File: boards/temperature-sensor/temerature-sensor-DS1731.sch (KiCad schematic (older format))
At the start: 2 parts

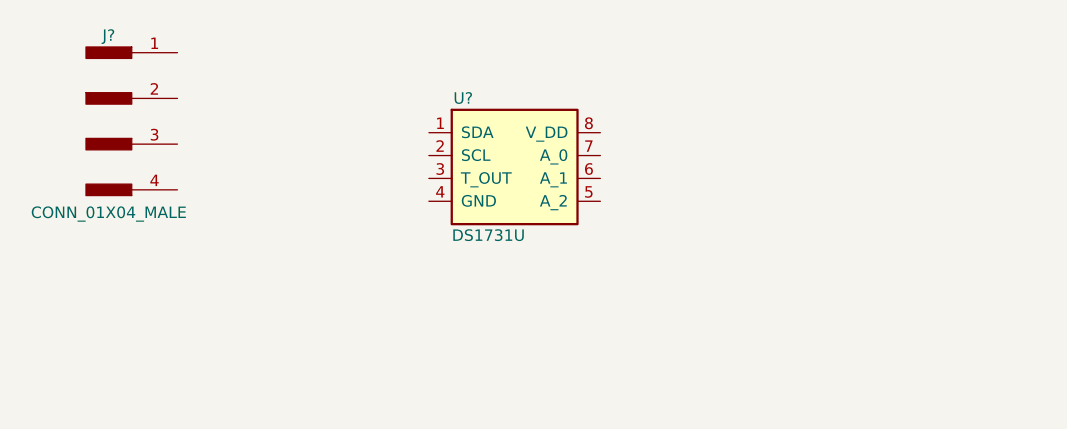
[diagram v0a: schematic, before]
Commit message: schematic completed
build the nessecary schematics, including a resistor Network to pull
address selector pins up or down using 0 and 10k resistors
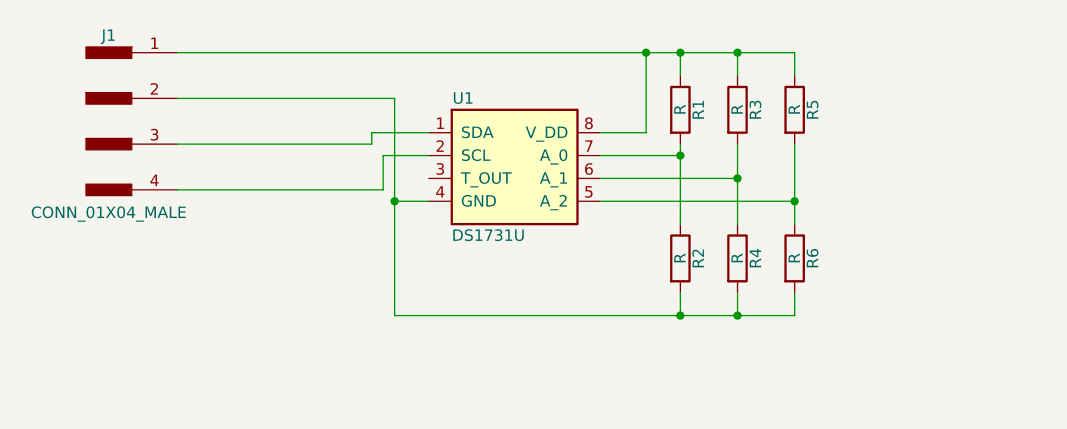
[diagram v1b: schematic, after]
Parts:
- added R1, R2, R3, R4, R5, R6: R, symbol R
- gave numbers to parts that had none: 2
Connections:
- net at U1.1 (SDA): now also J1.3
- net at U1.2 (SCL): now also J1.4
- net at U1.4 (GND): now also J1.2, R2.2, R4.2, R6.2
- net at U1.5 (A_2): now also R5.2, R6.1
- net at U1.6 (A_1): now also R3.2, R4.1
- net at U1.7 (A_0): now also R1.2, R2.1
- net at U1.8 (V_DD): now also J1.1, R1.1, R3.1, R5.1
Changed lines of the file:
@@
 LIBS:valves
 LIBS:rchojetzki-viper-temp-board
+LIBS:temerature-sensor-DS1731-cache
 EELAYER 25 0
 EELAYER END
@@
 $EndDescr
 $Comp
-L DS1731U U?
+L DS1731U U1
 U 1 1 58FF72EC
 P 2350 1700
-F 0 "U?" H 2200 2050 50  0000 C CNN
+F 0 "U1" H 2200 2050 50  0000 C CNN
 F 1 "DS1731U" H 2150 1450 50  0000 L CNN
 F 2 "" H 2250 1700 50  0001 C CNN
@@
 $EndComp
 $Comp
-L CONN_01X04_MALE J?
+L CONN_01X04_MALE J1
 U 1 1 58FF763C
 P 650 1450
-F 0 "J?" H 650 1825 50  0000 C CNN
+F 0 "J1" H 650 1825 50  0000 C CNN
 F 1 "CONN_01X04_MALE" H 650 1050 50  0000 C CNN
 F 2 "" H 650 1750 50  0001 C CNN
@@
 	1    0    0    -1
 $EndComp
+Wire Wire Line
+	950  1150 3650 1150
+Wire Wire Line
+	3000 1150 3000 1500
+Wire Wire Line
+	3000 1500 2800 1500
+Wire Wire Line
+	950  1350 1900 1350
+Wire Wire Line
+	1900 1350 1900 2300
+Wire Wire Line
+	1900 1800 2050 1800
+Wire Wire Line
+	2050 1600 1850 1600
+Wire Wire Line
+	1850 1600 1850 1750
+Wire Wire Line
+	1850 1750 950  1750
+Wire Wire Line
+	2050 1500 1800 1500
+Wire Wire Line
+	1800 1500 1800 1550
+Wire Wire Line
+	1800 1550 950  1550
+$Comp
+L R R1
+U 1 1 58FFD826
+P 3150 1400
+F 0 "R1" V 3230 1400 50  0000 C CNN
+F 1 "R" V 3150 1400 50  0000 C CNN
+F 2 "" V 3080 1400 50  0001 C CNN
+F 3 "" H 3150 1400 50  0001 C CNN
+	1    3150 1400
+	1    0    0    -1
+$EndComp
+$Comp
+L R R3
+U 1 1 58FFD8DE
+P 3400 1400
+F 0 "R3" V 3480 1400 50  0000 C CNN
+F 1 "R" V 3400 1400 50  0000 C CNN
+F 2 "" V 3330 1400 50  0001 C CNN
+F 3 "" H 3400 1400 50  0001 C CNN
+	1    3400 1400
+	1    0    0    -1
+$EndComp
+$Comp
+L R R5
+U 1 1 58FFD929
+P 3650 1400
+F 0 "R5" V 3730 1400 50  0000 C CNN
+F 1 "R" V 3650 1400 50  0000 C CNN
+F 2 "" V 3580 1400 50  0001 C CNN
+F 3 "" H 3650 1400 50  0001 C CNN
+	1    3650 1400
+	1    0    0    -1
+$EndComp
+Wire Wire Line
+	2800 1600 3150 1600
+Wire Wire Line
+	2800 1700 3400 1700
+Wire Wire Line
+	3400 1550 3400 1900
+Wire Wire Line
+	2800 1800 3650 1800
+Wire Wire Line
+	3650 1550 3650 1900
+Connection ~ 3000 1150
+Connection ~ 3150 1150
+Connection ~ 3400 1150
+$Comp
+L R R6
+U 1 1 58FFDA16
+P 3650 2050
+F 0 "R6" V 3730 2050 50  0000 C CNN
+F 1 "R" V 3650 2050 50  0000 C CNN
+F 2 "" V 3580 2050 50  0001 C CNN
+F 3 "" H 3650 2050 50  0001 C CNN
+	1    3650 2050
+	1    0    0    -1
+$EndComp
+$Comp
+L R R4
+U 1 1 58FFDAB6
+P 3400 2050
+F 0 "R4" V 3480 2050 50  0000 C CNN
+F 1 "R" V 3400 2050 50  0000 C CNN
+F 2 "" V 3330 2050 50  0001 C CNN
+F 3 "" H 3400 2050 50  0001 C CNN
+	1    3400 2050
+	1    0    0    -1
+$EndComp
+$Comp
+L R R2
+U 1 1 58FFDAFF
+P 3150 2050
+F 0 "R2" V 3230 2050 50  0000 C CNN
+F 1 "R" V 3150 2050 50  0000 C CNN
+F 2 "" V 3080 2050 50  0001 C CNN
+F 3 "" H 3150 2050 50  0001 C CNN
+	1    3150 2050
+	1    0    0    -1
+$EndComp
+Wire Wire Line
+	3150 1550 3150 1900
+Connection ~ 3400 1700
+Connection ~ 3650 1800
+Wire Wire Line
+	3650 1150 3650 1250
+Wire Wire Line
+	3400 1250 3400 1150
+Wire Wire Line
+	3150 1250 3150 1150
+Connection ~ 3150 1600
+Wire Wire Line
+	3650 2200 3650 2300
+Wire Wire Line
+	3650 2300 1900 2300
+Connection ~ 1900 1800
+Wire Wire Line
+	3400 2200 3400 2300
+Connection ~ 3400 2300
+Wire Wire Line
+	3150 2200 3150 2300
+Connection ~ 3150 2300
 $EndSCHEMATC

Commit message: pcb completed v1
needs review /
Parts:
- J1: footprint (none) -> Pin_Headers:Pin_Header_Straight_1x04_Pitch2.54mm
- R1, R2, R3, R4, R5, R6: footprint (none) -> Resistors_SMD:R_0603_HandSoldering
- U1: footprint (none) -> Housings_SOIC:SOIC-8-1EP_3.9x4.9mm_Pitch1.27mm
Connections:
- net SDA: now reaches J1.3, U1.1 (SDA)
- net SCL: now reaches J1.4, U1.2 (SCL)
- net GND: now reaches J1.2, R2.2, R4.2, R6.2, U1.4 (GND)
- net VDD: now reaches J1.1, R1.1, R3.1, R5.1, U1.8 (V_DD)
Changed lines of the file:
@@
 F 0 "U1" H 2200 2050 50  0000 C CNN
 F 1 "DS1731U" H 2150 1450 50  0000 L CNN
-F 2 "" H 2250 1700 50  0001 C CNN
+F 2 "Housings_SOIC:SOIC-8-1EP_3.9x4.9mm_Pitch1.27mm" H 2250 1700 50  0001 C CNN
 F 3 "" H 2350 1800 50  0001 C CNN
 	1    2350 1700
@@
 F 0 "J1" H 650 1825 50  0000 C CNN
 F 1 "CONN_01X04_MALE" H 650 1050 50  0000 C CNN
-F 2 "" H 650 1750 50  0001 C CNN
+F 2 "Pin_Headers:Pin_Header_Straight_1x04_Pitch2.54mm" H 650 1750 50  0001 C CNN
 F 3 "" H 650 1750 50  0001 C CNN
 	1    650  1450
@@
 F 0 "R1" V 3230 1400 50  0000 C CNN
 F 1 "R" V 3150 1400 50  0000 C CNN
-F 2 "" V 3080 1400 50  0001 C CNN
+F 2 "Resistors_SMD:R_0603_HandSoldering" V 3080 1400 50  0001 C CNN
 F 3 "" H 3150 1400 50  0001 C CNN
 	1    3150 1400
@@
 F 0 "R3" V 3480 1400 50  0000 C CNN
 F 1 "R" V 3400 1400 50  0000 C CNN
-F 2 "" V 3330 1400 50  0001 C CNN
+F 2 "Resistors_SMD:R_0603_HandSoldering" V 3330 1400 50  0001 C CNN
 F 3 "" H 3400 1400 50  0001 C CNN
 	1    3400 1400
@@
 F 0 "R5" V 3730 1400 50  0000 C CNN
 F 1 "R" V 3650 1400 50  0000 C CNN
-F 2 "" V 3580 1400 50  0001 C CNN
+F 2 "Resistors_SMD:R_0603_HandSoldering" V 3580 1400 50  0001 C CNN
 F 3 "" H 3650 1400 50  0001 C CNN
 	1    3650 1400
@@
 F 0 "R6" V 3730 2050 50  0000 C CNN
 F 1 "R" V 3650 2050 50  0000 C CNN
-F 2 "" V 3580 2050 50  0001 C CNN
+F 2 "Resistors_SMD:R_0603_HandSoldering" V 3580 2050 50  0001 C CNN
 F 3 "" H 3650 2050 50  0001 C CNN
 	1    3650 2050
@@
 F 0 "R4" V 3480 2050 50  0000 C CNN
 F 1 "R" V 3400 2050 50  0000 C CNN
-F 2 "" V 3330 2050 50  0001 C CNN
+F 2 "Resistors_SMD:R_0603_HandSoldering" V 3330 2050 50  0001 C CNN
 F 3 "" H 3400 2050 50  0001 C CNN
 	1    3400 2050
@@
 F 0 "R2" V 3230 2050 50  0000 C CNN
 F 1 "R" V 3150 2050 50  0000 C CNN
-F 2 "" V 3080 2050 50  0001 C CNN
+F 2 "Resistors_SMD:R_0603_HandSoldering" V 3080 2050 50  0001 C CNN
 F 3 "" H 3150 2050 50  0001 C CNN
 	1    3150 2050
@@
 	3150 2200 3150 2300
 Connection ~ 3150 2300
+Text Label 1000 1150 0    60   ~ 0
+VDD
+Text Label 1000 1350 0    60   ~ 0
+GND
+Text Label 1000 1550 0    60   ~ 0
+SDA
+Text Label 1000 1750 0    60   ~ 0
+SCL
 $EndSCHEMATC

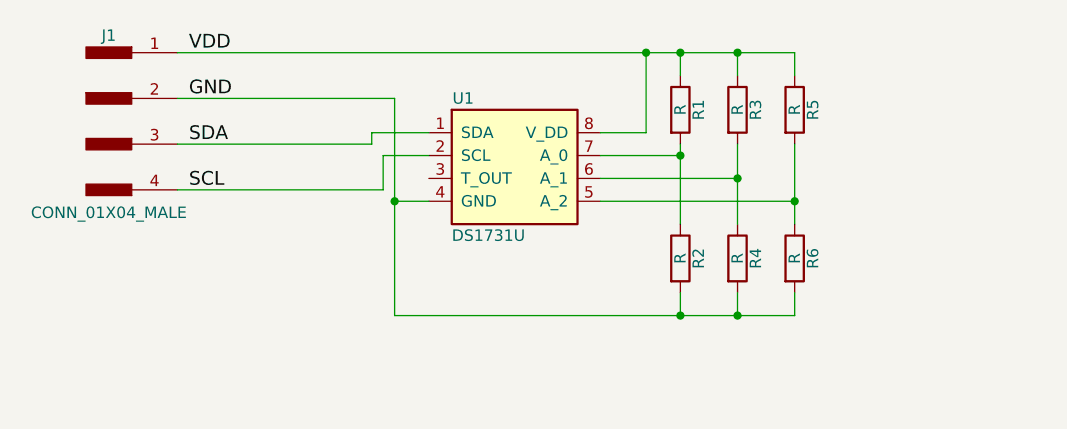
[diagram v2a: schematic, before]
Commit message: added solder-jumpers
the clearance at the jumpers looks prettey small,
is this allright?
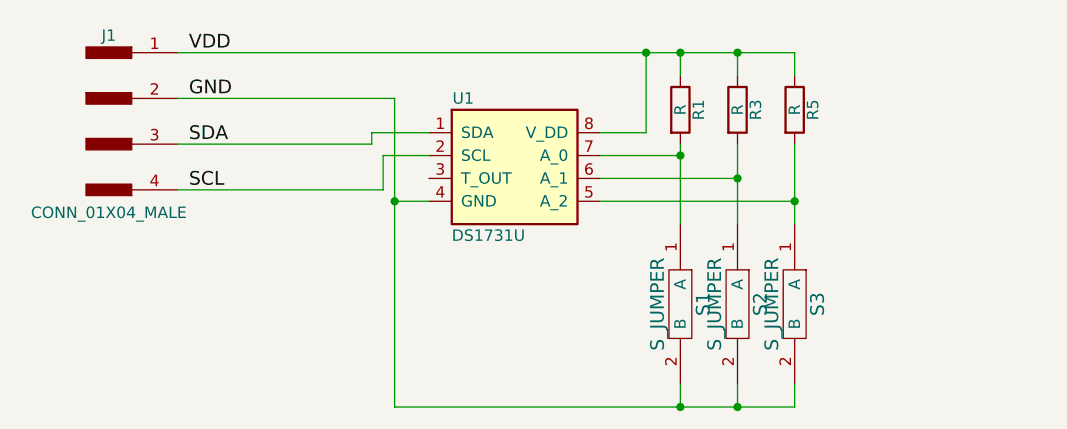
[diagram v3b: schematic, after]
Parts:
- removed R2, R4, R6: R, Resistors_SMD:R_0603_HandSoldering, symbol R
- added S1, S2, S3: S_JUMPER, rchojetzki-temp-board-footprint-lib:S_JUMPER_2_rchojetzki, symbol S_JUMPER
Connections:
- net GND: now also S1.2 (B), S2.2 (B), S3.2 (B)
- net at R5.2, U1.5 (A_2): now also S3.1 (A)
- net at R3.2, U1.6 (A_1): now also S2.1 (A)
- net at R1.2, U1.7 (A_0): now also S1.1 (A)
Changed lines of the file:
@@
 LIBS:valves
 LIBS:rchojetzki-viper-temp-board
+LIBS:open-project
 LIBS:temerature-sensor-DS1731-cache
 EELAYER 25 0
@@
 	950  1350 1900 1350
 Wire Wire Line
-	1900 1350 1900 2300
+	1900 1350 1900 2700
 Wire Wire Line
 	1900 1800 2050 1800
@@
 Connection ~ 3150 1150
 Connection ~ 3400 1150
-$Comp
-L R R6
-U 1 1 58FFDA16
-P 3650 2050
-F 0 "R6" V 3730 2050 50  0000 C CNN
-F 1 "R" V 3650 2050 50  0000 C CNN
-F 2 "Resistors_SMD:R_0603_HandSoldering" V 3580 2050 50  0001 C CNN
-F 3 "" H 3650 2050 50  0001 C CNN
-	1    3650 2050
-	1    0    0    -1
-$EndComp
-$Comp
-L R R4
-U 1 1 58FFDAB6
-P 3400 2050
-F 0 "R4" V 3480 2050 50  0000 C CNN
-F 1 "R" V 3400 2050 50  0000 C CNN
-F 2 "Resistors_SMD:R_0603_HandSoldering" V 3330 2050 50  0001 C CNN
-F 3 "" H 3400 2050 50  0001 C CNN
-	1    3400 2050
-	1    0    0    -1
-$EndComp
-$Comp
-L R R2
-U 1 1 58FFDAFF
-P 3150 2050
-F 0 "R2" V 3230 2050 50  0000 C CNN
-F 1 "R" V 3150 2050 50  0000 C CNN
-F 2 "Resistors_SMD:R_0603_HandSoldering" V 3080 2050 50  0001 C CNN
-F 3 "" H 3150 2050 50  0001 C CNN
-	1    3150 2050
-	1    0    0    -1
-$EndComp
 Wire Wire Line
 	3150 1550 3150 1900
@@
 	3150 1250 3150 1150
 Connection ~ 3150 1600
-Wire Wire Line
-	3650 2200 3650 2300
-Wire Wire Line
-	3650 2300 1900 2300
 Connection ~ 1900 1800
-Wire Wire Line
-	3400 2200 3400 2300
-Connection ~ 3400 2300
-Wire Wire Line
-	3150 2200 3150 2300
-Connection ~ 3150 2300
 Text Label 1000 1150 0    60   ~ 0
 VDD
@@
 Text Label 1000 1750 0    60   ~ 0
 SCL
+$Comp
+L S_JUMPER S1
+U 1 1 5902065C
+P 3400 2250
+F 0 "S1" H 3400 2100 60  0000 C CNN
+F 1 "S_JUMPER" H 3400 1900 60  0000 C CNN
+F 2 "rchojetzki-temp-board-footprint-lib:S_JUMPER_2_rchojetzki" H 3400 2250 60  0001 C CNN
+F 3 "" H 3400 2250 60  0001 C CNN
+	1    3400 2250
+	0    1    1    0
+$EndComp
+$Comp
+L S_JUMPER S2
+U 1 1 590206E5
+P 3650 2250
+F 0 "S2" H 3650 2100 60  0000 C CNN
+F 1 "S_JUMPER" H 3650 1900 60  0000 C CNN
+F 2 "rchojetzki-temp-board-footprint-lib:S_JUMPER_2_rchojetzki" H 3650 2250 60  0001 C CNN
+F 3 "" H 3650 2250 60  0001 C CNN
+	1    3650 2250
+	0    1    1    0
+$EndComp
+$Comp
+L S_JUMPER S3
+U 1 1 59020746
+P 3900 2250
+F 0 "S3" H 3900 2100 60  0000 C CNN
+F 1 "S_JUMPER" H 3900 1900 60  0000 C CNN
+F 2 "rchojetzki-temp-board-footprint-lib:S_JUMPER_2_rchojetzki" H 3900 2250 60  0001 C CNN
+F 3 "" H 3900 2250 60  0001 C CNN
+	1    3900 2250
+	0    1    1    0
+$EndComp
+Wire Wire Line
+	3150 2600 3150 2700
+Wire Wire Line
+	1900 2700 3650 2700
+Wire Wire Line
+	3400 2700 3400 2600
+Wire Wire Line
+	3650 2700 3650 2600
+Connection ~ 3400 2700
+Connection ~ 3150 2700
 $EndSCHEMATC

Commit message: boards/temperature_sensor: all complains addressed
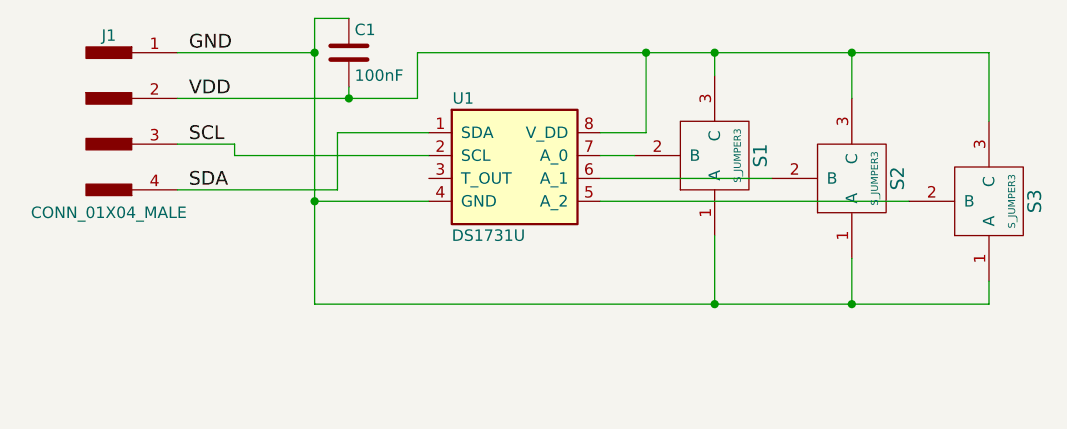
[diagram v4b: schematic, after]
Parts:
- removed R1, R3, R5: R, Resistors_SMD:R_0603_HandSoldering, symbol R
- removed S1, S2, S3: S_JUMPER, rchojetzki-temp-board-footprint-lib:S_JUMPER_2_rchojetzki, symbol S_JUMPER
- added C1: 100nF, Capacitors_SMD:C_0603_HandSoldering, symbol C
- added S1, S2, S3: S_JUMPER3, open-project:S_JUMPER_3, symbol S_JUMPER3
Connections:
- net GND: now also J1.1, C1.1, S1.1 (A), S2.1 (A), S3.1 (A); no longer J1.2
- net SCL: now also J1.3; no longer J1.4
- net SDA: now also J1.4; no longer J1.3
- net VDD: now also J1.2, C1.2, S1.3 (C), S2.3 (C), S3.3 (C); no longer J1.1
- net at U1.5 (A_2): now also S3.2 (B)
- net at U1.6 (A_1): now also S2.2 (B)
- net at U1.7 (A_0): now also S1.2 (B)
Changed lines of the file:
@@
 $EndComp
 Wire Wire Line
-	950  1150 3650 1150
+	3000 1500 2800 1500
+Text Label 1000 1150 0    60   ~ 0
+GND
+Text Label 1000 1350 0    60   ~ 0
+VDD
 Wire Wire Line
-	3000 1150 3000 1500
+	2950 1600 2800 1600
 Wire Wire Line
-	3000 1500 2800 1500
+	3550 1700 2800 1700
 Wire Wire Line
-	950  1350 1900 1350
-Wire Wire Line
-	1900 1350 1900 2700
-Wire Wire Line
-	1900 1800 2050 1800
-Wire Wire Line
-	2050 1600 1850 1600
-Wire Wire Line
-	1850 1600 1850 1750
-Wire Wire Line
-	1850 1750 950  1750
-Wire Wire Line
-	2050 1500 1800 1500
-Wire Wire Line
-	1800 1500 1800 1550
-Wire Wire Line
-	1800 1550 950  1550
+	4150 1800 2800 1800
 $Comp
-L R R1
-U 1 1 58FFD826
-P 3150 1400
-F 0 "R1" V 3230 1400 50  0000 C CNN
-F 1 "R" V 3150 1400 50  0000 C CNN
-F 2 "Resistors_SMD:R_0603_HandSoldering" V 3080 1400 50  0001 C CNN
-F 3 "" H 3150 1400 50  0001 C CNN
-	1    3150 1400
-	1    0    0    -1
-$EndComp
-$Comp
-L R R3
-U 1 1 58FFD8DE
-P 3400 1400
-F 0 "R3" V 3480 1400 50  0000 C CNN
-F 1 "R" V 3400 1400 50  0000 C CNN
-F 2 "Resistors_SMD:R_0603_HandSoldering" V 3330 1400 50  0001 C CNN
-F 3 "" H 3400 1400 50  0001 C CNN
-	1    3400 1400
-	1    0    0    -1
-$EndComp
-$Comp
-L R R5
-U 1 1 58FFD929
-P 3650 1400
-F 0 "R5" V 3730 1400 50  0000 C CNN
-F 1 "R" V 3650 1400 50  0000 C CNN
-F 2 "Resistors_SMD:R_0603_HandSoldering" V 3580 1400 50  0001 C CNN
-F 3 "" H 3650 1400 50  0001 C CNN
-	1    3650 1400
+L C C1
+U 1 1 591086F1
+P 1700 1150
+F 0 "C1" H 1725 1250 50  0000 L CNN
+F 1 "100nF" H 1725 1050 50  0000 L CNN
+F 2 "Capacitors_SMD:C_0603_HandSoldering" H 1738 1000 50  0001 C CNN
+F 3 "" H 1700 1150 50  0001 C CNN
+	1    1700 1150
 	1    0    0    -1
 $EndComp
 Wire Wire Line
-	2800 1600 3150 1600
+	1550 2250 4500 2250
 Wire Wire Line
-	2800 1700 3400 1700
+	4500 2250 4500 2150
 Wire Wire Line
-	3400 1550 3400 1900
+	3900 2050 3900 2250
+Connection ~ 3900 2250
 Wire Wire Line
-	2800 1800 3650 1800
+	3300 1950 3300 2250
+Connection ~ 3300 2250
 Wire Wire Line
-	3650 1550 3650 1900
+	4500 1150 4500 1450
+Wire Wire Line
+	3900 1350 3900 1150
+Connection ~ 3900 1150
+Wire Wire Line
+	3300 1250 3300 1150
+Connection ~ 3300 1150
+Wire Wire Line
+	3000 1500 3000 1150
 Connection ~ 3000 1150
-Connection ~ 3150 1150
-Connection ~ 3400 1150
 Wire Wire Line
-	3150 1550 3150 1900
-Connection ~ 3400 1700
-Connection ~ 3650 1800
-Wire Wire Line
-	3650 1150 3650 1250
-Wire Wire Line
-	3400 1250 3400 1150
-Wire Wire Line
-	3150 1250 3150 1150
-Connection ~ 3150 1600
-Connection ~ 1900 1800
-Text Label 1000 1150 0    60   ~ 0
-VDD
-Text Label 1000 1350 0    60   ~ 0
-GND
-Text Label 1000 1550 0    60   ~ 0
-SDA
-Text Label 1000 1750 0    60   ~ 0
-SCL
+	950  1350 2000 1350
 $Comp
-L S_JUMPER S1
-U 1 1 5902065C
-P 3400 2250
-F 0 "S1" H 3400 2100 60  0000 C CNN
-F 1 "S_JUMPER" H 3400 1900 60  0000 C CNN
-F 2 "rchojetzki-temp-board-footprint-lib:S_JUMPER_2_rchojetzki" H 3400 2250 60  0001 C CNN
-F 3 "" H 3400 2250 60  0001 C CNN
-	1    3400 2250
-	0    1    1    0
+L S_JUMPER3 S1
+U 1 1 5910A1C4
+P 3300 1600
+F 0 "S1" V 3100 1600 60  0000 C CNN
+F 1 "S_JUMPER3" V 3200 1600 31  0000 C CNN
+F 2 "open-project:S_JUMPER_3" H 3300 1600 60  0001 C CNN
+F 3 "" H 3300 1600 60  0001 C CNN
+	1    3300 1600
+	-1   0    0    1
 $EndComp
 $Comp
-L S_JUMPER S2
-U 1 1 590206E5
-P 3650 2250
-F 0 "S2" H 3650 2100 60  0000 C CNN
-F 1 "S_JUMPER" H 3650 1900 60  0000 C CNN
-F 2 "rchojetzki-temp-board-footprint-lib:S_JUMPER_2_rchojetzki" H 3650 2250 60  0001 C CNN
-F 3 "" H 3650 2250 60  0001 C CNN
-	1    3650 2250
-	0    1    1    0
+L S_JUMPER3 S2
+U 1 1 5910A375
+P 3900 1700
+F 0 "S2" V 3700 1700 60  0000 C CNN
+F 1 "S_JUMPER3" V 3800 1700 31  0000 C CNN
+F 2 "open-project:S_JUMPER_3" H 3900 1700 60  0001 C CNN
+F 3 "" H 3900 1700 60  0001 C CNN
+	1    3900 1700
+	-1   0    0    1
 $EndComp
 $Comp
-L S_JUMPER S3
-U 1 1 59020746
-P 3900 2250
-F 0 "S3" H 3900 2100 60  0000 C CNN
-F 1 "S_JUMPER" H 3900 1900 60  0000 C CNN
-F 2 "rchojetzki-temp-board-footprint-lib:S_JUMPER_2_rchojetzki" H 3900 2250 60  0001 C CNN
-F 3 "" H 3900 2250 60  0001 C CNN
-	1    3900 2250
-	0    1    1    0
+L S_JUMPER3 S3
+U 1 1 5910A463
+P 4500 1800
+F 0 "S3" V 4300 1800 60  0000 C CNN
+F 1 "S_JUMPER3" V 4400 1800 31  0000 C CNN
+F 2 "open-project:S_JUMPER_3" H 4500 1800 60  0001 C CNN
+F 3 "" H 4500 1800 60  0001 C CNN
+	1    4500 1800
+	-1   0    0    1
 $EndComp
 Wire Wire Line
-	3150 2600 3150 2700
+	2050 1600 1200 1600
 Wire Wire Line
-	1900 2700 3650 2700
+	1200 1600 1200 1550
 Wire Wire Line
-	3400 2700 3400 2600
+	1200 1550 950  1550
 Wire Wire Line
-	3650 2700 3650 2600
-Connection ~ 3400 2700
-Connection ~ 3150 2700
+	950  1750 1650 1750
+Text Label 1000 1550 0    60   ~ 0
+SCL
+Text Label 1000 1750 0    60   ~ 0
+SDA
+Wire Wire Line
+	2050 1500 1650 1500
+Wire Wire Line
+	1650 1500 1650 1750
+Wire Wire Line
+	950  1150 1550 1150
+Wire Wire Line
+	1550 1800 2050 1800
+Wire Wire Line
+	1550 1000 1550 2250
+Connection ~ 1550 1800
+Wire Wire Line
+	2000 1350 2000 1150
+Wire Wire Line
+	2000 1150 4500 1150
+Wire Wire Line
+	1700 1300 1700 1350
+Connection ~ 1700 1350
+Wire Wire Line
+	1550 1000 1700 1000
+Connection ~ 1550 1150
 $EndSCHEMATC
